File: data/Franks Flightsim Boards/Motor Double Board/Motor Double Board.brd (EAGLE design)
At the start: 80 x 77.8 mm, 27 parts, among them IC1 A1202UA, IC2 A1202UA, IC3-VID6606 VID66-06, J4 LEDS, J5 22-27-2041-04, J6 22-27-2041-04, SW1 EC12E_SW, SW2 EC12E_SW, X1 BUS

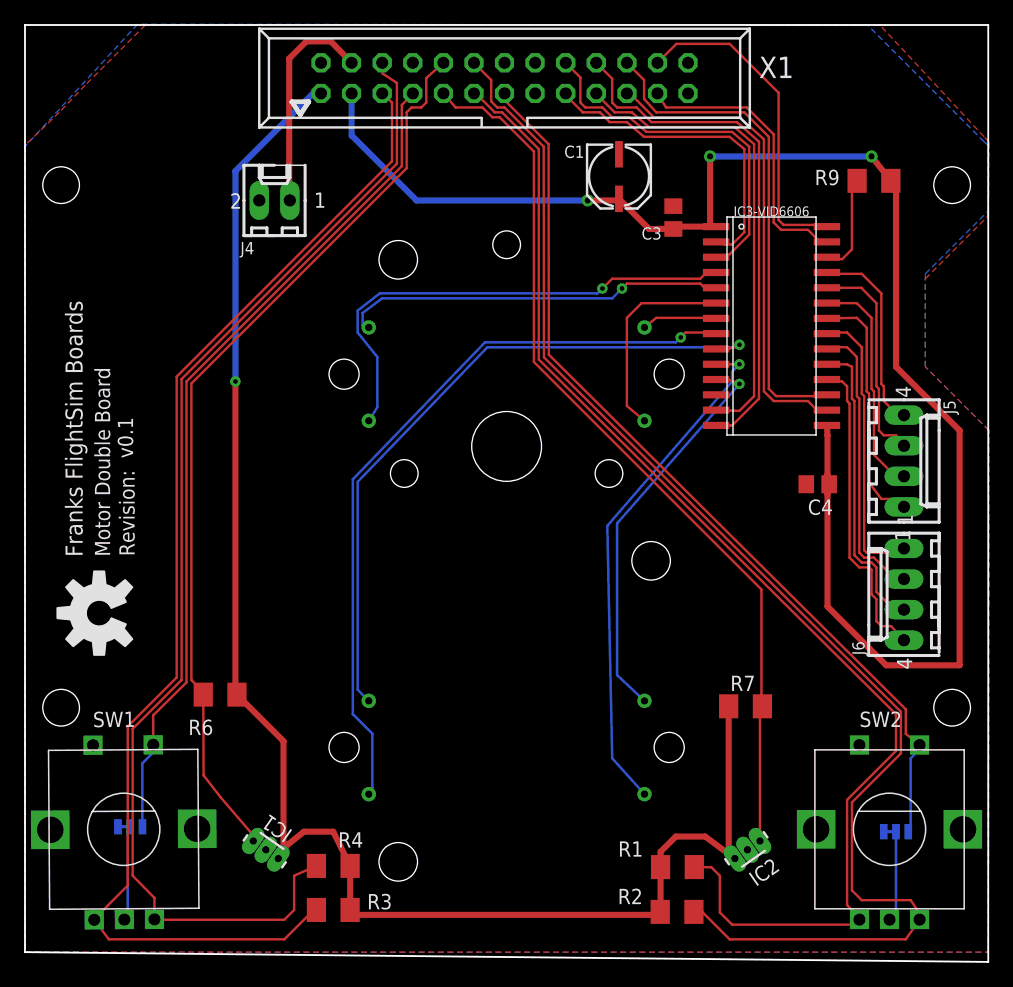
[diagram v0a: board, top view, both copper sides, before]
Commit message: new PCB
Updated with new pcb for 2_25 version
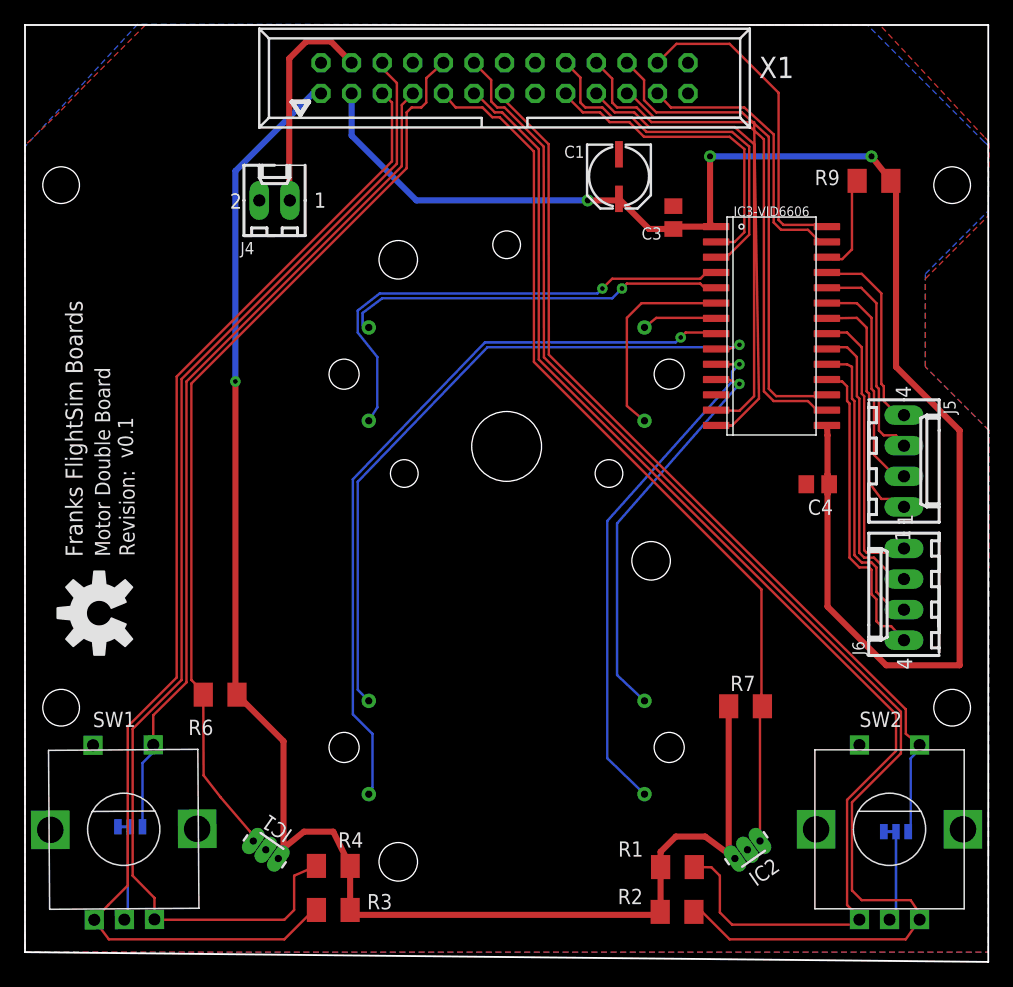
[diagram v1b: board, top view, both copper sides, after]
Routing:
- net STEPC: track 43.6 -> 44.2 mm
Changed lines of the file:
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@@
 <wire x1="46.5328" y1="73.152" x2="47.9552" y2="73.152" width="0.2032" layer="1"/>
 <wire x1="47.9552" y1="73.152" x2="48.768" y2="72.3392" width="0.2032" layer="1"/>
-<wire x1="48.768" y1="72.3392" x2="50.1904" y2="72.3392" width="0.2032" layer="1"/>
-<wire x1="50.1904" y1="72.3392" x2="51.6128" y2="71.12" width="0.2032" layer="1"/>
+<wire x1="48.768" y1="72.3392" x2="50.3936" y2="72.3392" width="0.2032" layer="1"/>
+<wire x1="50.3936" y1="72.3392" x2="51.6128" y2="71.12" width="0.2032" layer="1"/>
 <wire x1="51.6128" y1="71.12" x2="58.7248" y2="71.12" width="0.2032" layer="1"/>
 <wire x1="58.7248" y1="71.12" x2="60.1472" y2="69.9008" width="0.2032" layer="1"/>
@@
 <wire x1="62.7888" y1="62.992" x2="62.1792" y2="63.6016" width="0.2032" layer="1"/>
 <wire x1="62.1792" y1="63.6016" x2="62.1792" y2="70.9168" width="0.2032" layer="1"/>
-<wire x1="62.1792" y1="70.9168" x2="59.944" y2="73.152" width="0.2032" layer="1"/>
+<wire x1="62.1792" y1="70.9168" x2="59.7408" y2="73.152" width="0.2032" layer="1"/>
 <contactref element="X1" pad="23"/>
-<wire x1="52.5272" y1="74.3204" x2="53.2384" y2="73.152" width="0.2032" layer="1"/>
-<wire x1="53.2384" y1="73.152" x2="59.944" y2="73.152" width="0.2032" layer="1"/>
+<wire x1="52.5272" y1="74.3204" x2="53.6448" y2="73.152" width="0.2032" layer="1"/>
+<wire x1="53.6448" y1="73.152" x2="59.7408" y2="73.152" width="0.2032" layer="1"/>
 </signal>
 <signal name="OUT2A">
@@
 <contactref element="X1" pad="6"/>
 <wire x1="30.8864" y1="75.184" x2="30.8864" y2="68.4784" width="0.2032" layer="1"/>
-<wire x1="30.8864" y1="75.184" x2="29.6672" y2="75.9968" width="0.2032" layer="1"/>
-<wire x1="29.6672" y1="75.9968" x2="29.6672" y2="76.8604" width="0.2032" layer="1"/>
+<wire x1="30.8864" y1="75.184" x2="29.6672" y2="76.4032" width="0.2032" layer="1"/>
+<wire x1="29.6672" y1="76.4032" x2="29.6672" y2="76.8604" width="0.2032" layer="1"/>
 </signal>
 <signal name="RE1_B">
@@
 <wire x1="59.3344" y1="51.816" x2="58.1152" y2="51.816" width="0.2032" layer="1"/>
 <wire x1="58.1152" y1="51.816" x2="57.4" y2="51.825" width="0.2032" layer="1"/>
-<wire x1="48.3616" y1="38.4048" x2="58.7248" y2="50.3936" width="0.2032" layer="16"/>
-<wire x1="48.768" y1="19.1008" x2="48.3616" y2="38.4048" width="0.2032" layer="16"/>
-<wire x1="48.768" y1="19.1008" x2="51.45" y2="16.12" width="0.2032" layer="16"/>
+<wire x1="48.3616" y1="38.8112" x2="58.7248" y2="50.3936" width="0.2032" layer="16"/>
+<wire x1="48.3616" y1="19.1008" x2="48.3616" y2="38.8112" width="0.2032" layer="16"/>
+<wire x1="48.3616" y1="19.1008" x2="51.45" y2="16.12" width="0.2032" layer="16"/>
 <via x="59.3344" y="51.816" extent="1-16" drill="0.381"/>
 </signal>
@@
 <wire x1="58.5216" y1="46.736" x2="58.7248" y2="46.736" width="0.2032" layer="1"/>
 <wire x1="58.7248" y1="46.736" x2="60.96" y2="48.9712" width="0.2032" layer="1"/>
-<wire x1="60.96" y1="48.9712" x2="60.96" y2="70.3072" width="0.2032" layer="1"/>
-<wire x1="60.96" y1="70.3072" x2="59.1312" y2="71.9328" width="0.2032" layer="1"/>
-<wire x1="59.1312" y1="71.9328" x2="52.0192" y2="71.9328" width="0.2032" layer="1"/>
+<wire x1="60.96" y1="48.9712" x2="60.5536" y2="71.9328" width="0.2032" layer="1"/>
+<wire x1="60.5536" y1="71.9328" x2="52.0192" y2="71.9328" width="0.2032" layer="1"/>
 <wire x1="52.0192" y1="71.9328" x2="50.8" y2="73.152" width="0.2032" layer="1"/>
 <wire x1="49.1744" y1="73.152" x2="50.8" y2="73.152" width="0.2032" layer="1"/>
@@
 <wire x1="65.8368" y1="49.1744" x2="62.3824" y2="49.1744" width="0.2032" layer="1"/>
 <wire x1="62.3824" y1="49.1744" x2="61.7728" y2="49.784" width="0.2032" layer="1"/>
-<wire x1="59.7408" y1="72.7456" x2="61.7728" y2="70.7136" width="0.2032" layer="1"/>
-<wire x1="52.4256" y1="72.7456" x2="59.7408" y2="72.7456" width="0.2032" layer="1"/>
+<wire x1="59.5376" y1="72.7456" x2="61.7728" y2="70.7136" width="0.2032" layer="1"/>
+<wire x1="52.4256" y1="72.7456" x2="59.5376" y2="72.7456" width="0.2032" layer="1"/>
 <wire x1="61.7728" y1="70.7136" x2="61.7728" y2="49.784" width="0.2032" layer="1"/>
 <contactref element="X1" pad="22"/>
-<wire x1="51.4176" y1="73.8607875" x2="52.4256" y2="72.7456" width="0.2032" layer="1"/>
+<wire x1="51.4096" y1="73.7616" x2="52.4256" y2="72.7456" width="0.2032" layer="1"/>
 <wire x1="49.9872" y1="76.8604" x2="51.4176" y2="75.43" width="0.2032" layer="1"/>
-<wire x1="51.4176" y1="75.43" x2="51.4176" y2="73.8607875" width="0.2032" layer="1"/>
+<wire x1="51.4176" y1="75.43" x2="51.4096" y2="73.7616" width="0.2032" layer="1"/>
 </signal>
 <signal name="DIRB">
 <contactref element="IC3-VID6606" pad="2"/>
-<wire x1="57.4" y1="61.985" x2="58.1152" y2="61.7728" width="0.2032" layer="1"/>
-<wire x1="58.1152" y1="61.7728" x2="58.7248" y2="61.7728" width="0.2032" layer="1"/>
-<wire x1="58.7248" y1="61.7728" x2="59.7408" y2="62.7888" width="0.2032" layer="1"/>
+<wire x1="57.4" y1="61.985" x2="57.912" y2="61.976" width="0.2032" layer="1"/>
+<wire x1="57.912" y1="61.976" x2="58.928" y2="61.976" width="0.2032" layer="1"/>
+<wire x1="58.928" y1="61.976" x2="59.7408" y2="62.7888" width="0.2032" layer="1"/>
 <wire x1="59.7408" y1="69.6976" x2="58.5216" y2="70.7136" width="0.2032" layer="1"/>
 <wire x1="58.5216" y1="70.7136" x2="51.4096" y2="70.7136" width="0.2032" layer="1"/>
-<wire x1="51.4096" y1="70.7136" x2="49.9872" y2="71.9328" width="0.2032" layer="1"/>
-<wire x1="49.9872" y1="71.9328" x2="48.5648" y2="71.9328" width="0.2032" layer="1"/>
+<wire x1="51.4096" y1="70.7136" x2="50.1904" y2="71.9328" width="0.2032" layer="1"/>
+<wire x1="50.1904" y1="71.9328" x2="48.5648" y2="71.9328" width="0.2032" layer="1"/>
 <wire x1="48.5648" y1="71.9328" x2="47.752" y2="72.7456" width="0.2032" layer="1"/>
 <wire x1="47.752" y1="72.7456" x2="46.3296" y2="72.7456" width="0.2032" layer="1"/>
@@
 <wire x1="60.5536" y1="70.104" x2="58.928" y2="71.5264" width="0.2032" layer="1"/>
 <wire x1="58.928" y1="71.5264" x2="51.816" y2="71.5264" width="0.2032" layer="1"/>
-<wire x1="51.816" y1="71.5264" x2="50.3936" y2="72.7456" width="0.2032" layer="1"/>
-<wire x1="48.9712" y1="72.7456" x2="50.3936" y2="72.7456" width="0.2032" layer="1"/>
+<wire x1="51.816" y1="71.5264" x2="50.5968" y2="72.7456" width="0.2032" layer="1"/>
+<wire x1="48.9712" y1="72.7456" x2="50.5968" y2="72.7456" width="0.2032" layer="1"/>
 <wire x1="60.5536" y1="49.1744" x2="60.5536" y2="70.104" width="0.2032" layer="1"/>
 <contactref element="X1" pad="19"/>
